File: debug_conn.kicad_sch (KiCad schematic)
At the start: 1 part, among them J3 Conn_01x06_Pin

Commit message: stuff
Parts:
- added TP100, TP101, TP102, TP103, TP99: TestPoint, symbol Connector:TestPoint
- J3: footprint (none) -> Connector_PinHeader_2.54mm:PinHeader_1x06_P2.54mm_Vertical
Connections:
- net UART.RX: now also TP102.1
- net UART.TX: now also TP101.1
- net NC_DBG_UART_VCC: now reaches J3.3 (Pin_3)
- net NC_DBG_UART_VCC: now also TP100.1
- net UART.CTS# renamed NC_DBG_UART_CTS#
- net NC_DBG_UART_CTS#: now also TP99.1
- net UART.RTS# renamed NC_DBG_UART_RTS#
- net NC_DBG_UART_RTS#: now also TP103.1
- no-connect marks 1 -> 0
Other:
- note added: "TODO: check what the small jtag connector is called"

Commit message: did stuff
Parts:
- renumbered TP99 to TP128, TP100 to TP129, TP101 to TP130, TP102 to TP131, TP103 to TP132
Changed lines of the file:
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@@
 		(dnp no)
 		(fields_autoplaced yes)
-		(property "Reference" "#PWR080"
+		(property "Reference" "#PWR0177"
 			(at 153.67 62.23 0)
 			(effects
@@
 			(project ""
 				(path "/2970f661-65ab-4e2b-aeda-d76d1044f2b8/3126208c-7808-4087-8557-46cefae30ae4"
-					(reference "#PWR080")
+					(reference "#PWR0177")
 					(unit 1)
 				)
@@
 		(on_board yes)
 		(dnp no)
-		(property "Reference" "TP103"
+		(property "Reference" "TP132"
 			(at 142.494 75.184 90)
 			(effects
@@
 			(project "netdaq"
 				(path "/2970f661-65ab-4e2b-aeda-d76d1044f2b8/3126208c-7808-4087-8557-46cefae30ae4"
-					(reference "TP103")
+					(reference "TP132")
 					(unit 1)
 				)
@@
 		(on_board yes)
 		(dnp no)
-		(property "Reference" "TP102"
+		(property "Reference" "TP131"
 			(at 142.494 72.644 90)
 			(effects
@@
 			(project "netdaq"
 				(path "/2970f661-65ab-4e2b-aeda-d76d1044f2b8/3126208c-7808-4087-8557-46cefae30ae4"
-					(reference "TP102")
+					(reference "TP131")
 					(unit 1)
 				)
@@
 		(on_board yes)
 		(dnp no)
-		(property "Reference" "TP100"
+		(property "Reference" "TP129"
 			(at 142.494 67.564 90)
 			(effects
@@
 			(project "netdaq"
 				(path "/2970f661-65ab-4e2b-aeda-d76d1044f2b8/3126208c-7808-4087-8557-46cefae30ae4"
-					(reference "TP100")
+					(reference "TP129")
 					(unit 1)
 				)
@@
 		(on_board yes)
 		(dnp no)
-		(property "Reference" "TP101"
+		(property "Reference" "TP130"
 			(at 142.494 70.104 90)
 			(effects
@@
 			(project "netdaq"
 				(path "/2970f661-65ab-4e2b-aeda-d76d1044f2b8/3126208c-7808-4087-8557-46cefae30ae4"
-					(reference "TP101")
+					(reference "TP130")
 					(unit 1)
 				)
@@
 		(on_board yes)
 		(dnp no)
-		(property "Reference" "TP99"
+		(property "Reference" "TP128"
 			(at 142.494 65.024 90)
 			(effects
@@
 			(project "netdaq"
 				(path "/2970f661-65ab-4e2b-aeda-d76d1044f2b8/3126208c-7808-4087-8557-46cefae30ae4"
-					(reference "TP99")
-					(unit 1)
-				)
+					(reference "TP128")
+					(unit 1)
+				)

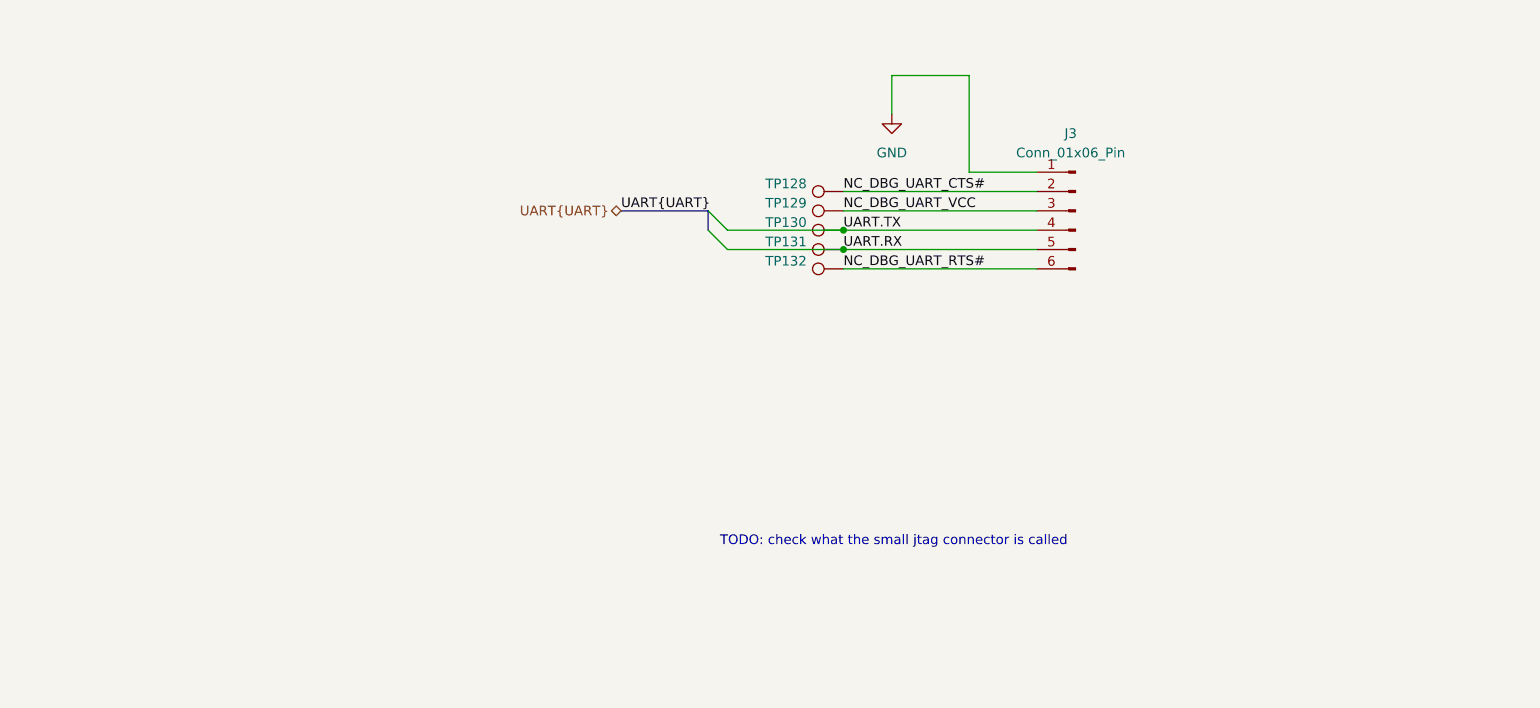
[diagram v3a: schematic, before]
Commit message: changed to 4 layer, finished usb conn, added jtag conn, some other things
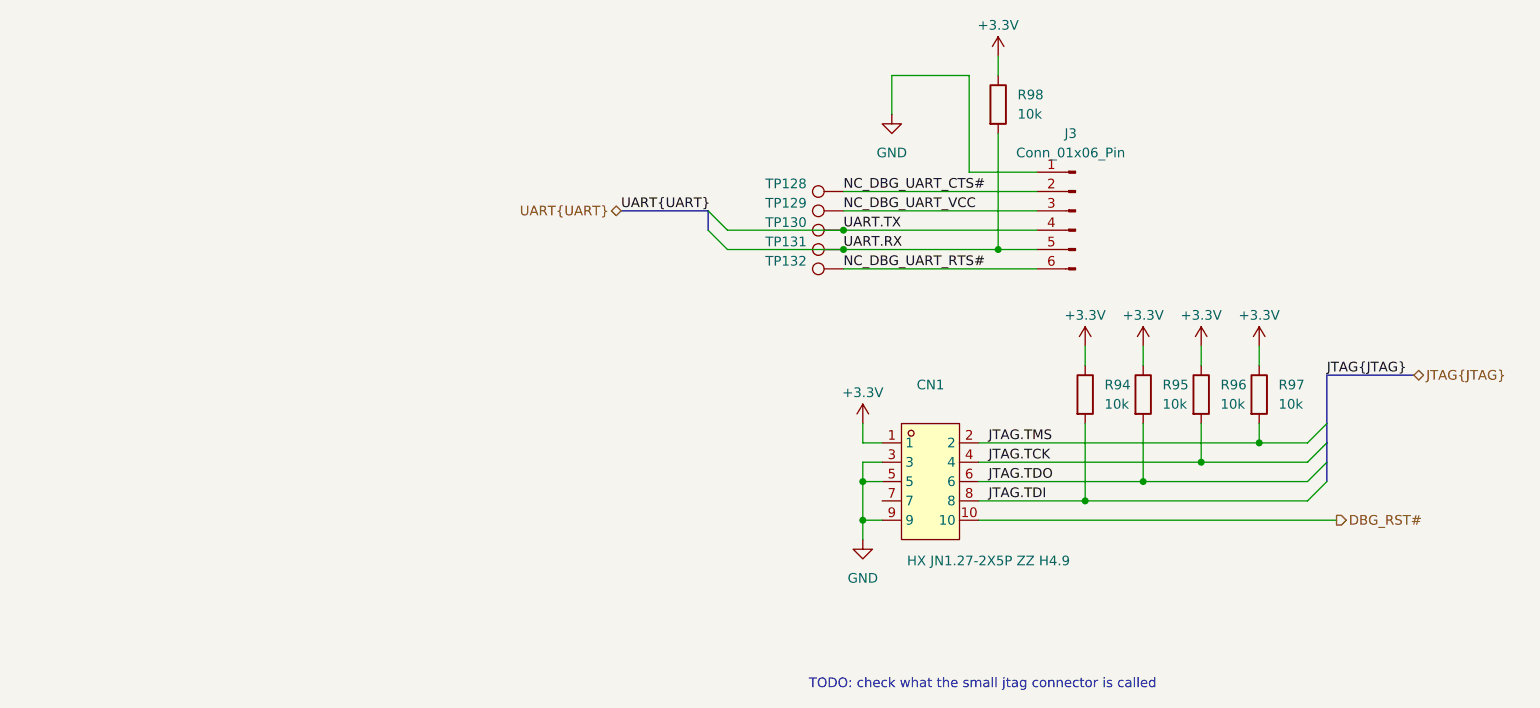
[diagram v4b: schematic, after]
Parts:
- added CN1: HX JN1.27-2X5P ZZ H4.9, C42372547:CONN-TH_10P-P1.27_HX-JN1.27-2X5P-ZZ-H4.9, symbol C42372547:HXJN1.27-2X5PZZH4.9
- added R94, R95, R96, R97, R98: 10k, Resistor_SMD:R_0402_1005Metric, symbol Device:R
- TP128, TP129, TP130, TP131, TP132: footprint (none) -> TestPoint:TestPoint_THTPad_D1.0mm_Drill0.5mm
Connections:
- net GND: now also CN1.3, CN1.5, CN1.9
- net UART.RX: now also R98.2
- new net +3.3V: CN1.1, R94.1, R95.1, R96.1, R97.1, R98.1
- new net DBG_RST#: CN1.10
- new net JTAG.TCK: CN1.4, R96.2
- new net JTAG.TDI: CN1.8, R94.2
- new net JTAG.TDO: CN1.6, R95.2
- new net JTAG.TMS: CN1.2, R97.2

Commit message: many stuffs
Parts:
- added C129, C130: 100n, Capacitor_SMD:C_0402_1005Metric, symbol Device:C
- added TP182: TestPoint_Alt, TestPoint:TestPoint_THTPad_1.0x1.0mm_Drill0.5mm, symbol Connector:TestPoint_Alt
- added U14: TXU0202DCUR, C5186957:VSSOP-8_L2.3-W2.0-P0.50-LS3.1-BR, symbol C5186957:TXU0202DCUR
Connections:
- net +3.3V: now also C129.1, U14.3 (VCCA), U14.6 (OE)
- net GND: now also C129.2, C130.2, TP182.1, U14.2 (GND)
- net UART.RX: now also U14.4 (A2Y); no longer J3.5 (Pin_5)
- net UART.TX: now also U14.5 (A1); no longer J3.4 (Pin_4)
- net NC_DBG_UART_CTS# renamed NC_UART_CTS#
- net NC_DBG_UART_RTS# renamed NC_UART_RTS#
- net NC_DBG_UART_VCC renamed EXT_UART_VCC
- net EXT_UART_VCC: now also C130.1, U14.7 (VCCB)
- new net EXT_UART_RX: J3.5 (Pin_5), U14.1 (B2)
- new net EXT_UART_TX: J3.4 (Pin_4), U14.8 (B1Y)

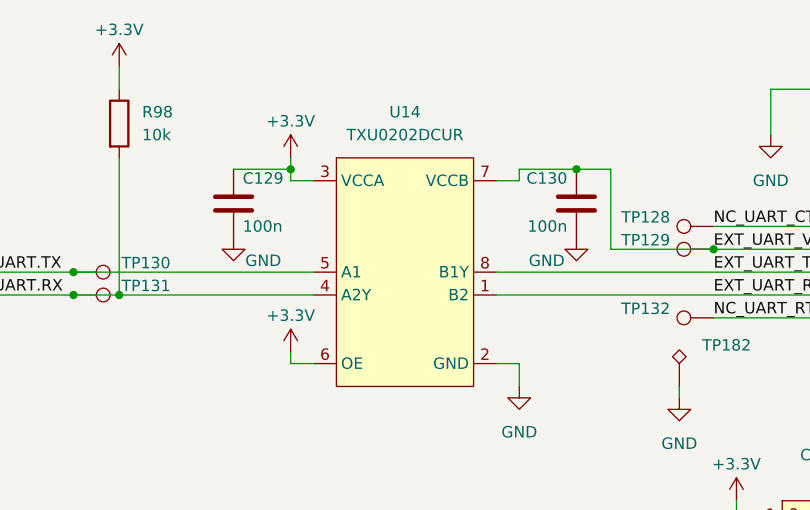
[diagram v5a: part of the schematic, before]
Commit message: did a bunch of bom matching to lcsc
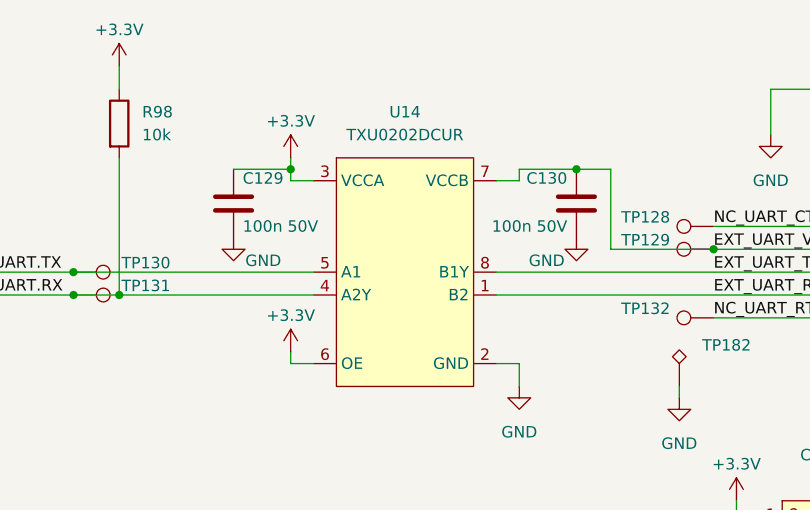
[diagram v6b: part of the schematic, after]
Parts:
- C129, C130: value 100n -> 100n 50V; LCSC (none) -> C307331; LCSC Basic/Pref (none) -> x; LCSC Part (none) -> C307331
- R94, R95, R96, R97, R98: LCSC (none) -> C25744; LCSC Basic/Pref (none) -> x; LCSC Part (none) -> C25744
- TP128, TP129, TP130, TP131, TP132, TP182: now left out of the parts list
